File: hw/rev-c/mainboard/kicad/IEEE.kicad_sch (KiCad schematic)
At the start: 26 parts, among them J1 IEEE, J14 IEEE_HEADER, U14 SN74LS07, U15 SN74LS07, U16 SN74LS07, U17 74LS245, U18 74LS245

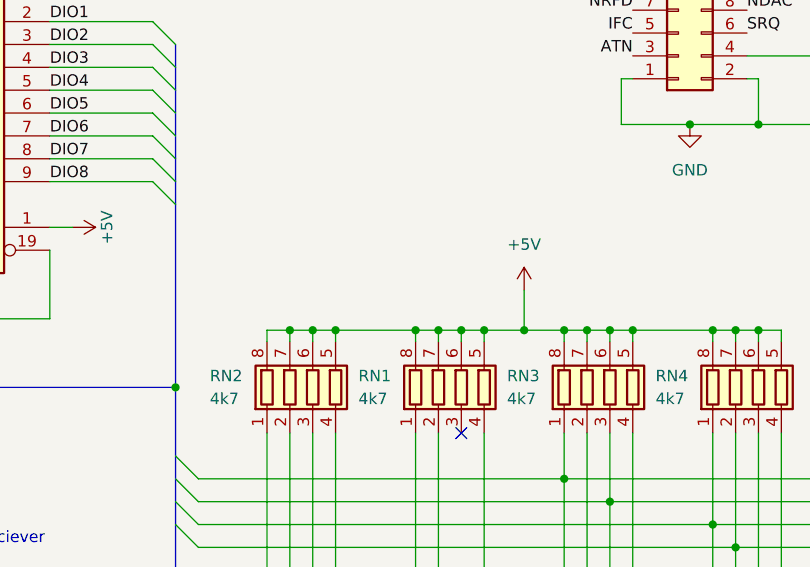
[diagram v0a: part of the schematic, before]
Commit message: hw: fix wire/grid violations in schematic
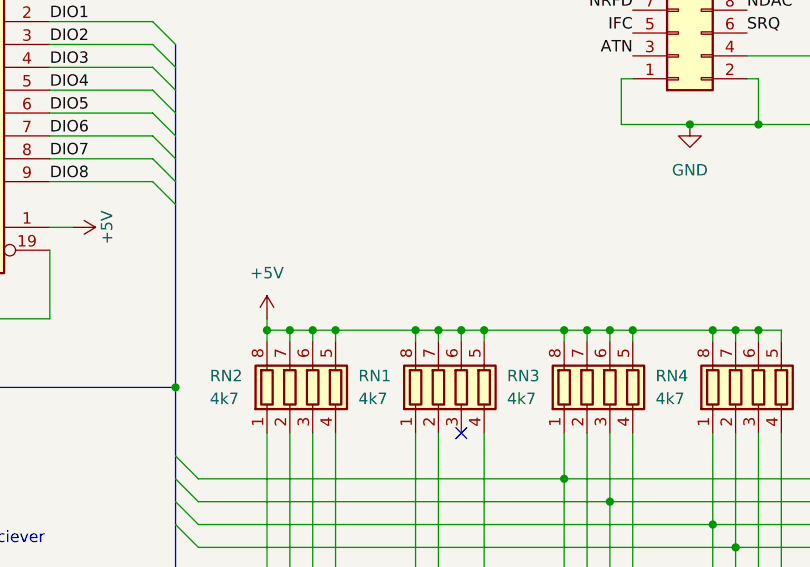
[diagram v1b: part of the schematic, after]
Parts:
- J1: symbol Retrocomputing:CBM_PET_IEEE_Conn_02x12_Card_Edge -> EconoPET:CBM_PET_IEEE_Conn_02x12_Card_Edge
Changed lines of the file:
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@@
 	)
 	(junction
-		(at 193.675 72.39)
-		(diameter 0)
-		(color 0 0 0 0)
-	)
-	(junction
 		(at 181.61 72.39)
 		(diameter 0)
@@
 	)
 	(junction
+		(at 165.1 72.39)
+		(diameter 0)
+		(color 0 0 0 0)
+	)
+	(junction
 		(at 198.12 88.9)
 		(diameter 0)
@@
 	(wire
 		(pts
+			(xy 165.1 72.39) (xy 167.64 72.39)
+		)
+		(stroke
+			(width 0)
+			(type default)
+		)
+	)
+	(wire
+		(pts
 			(xy 214.63 83.82) (xy 214.63 93.98)
 		)
@@
 		)
 	)
-	(wire
-		(pts
-			(xy 186.69 72.39) (xy 189.23 72.39)
-		)
-		(stroke
-			(width 0)
-			(type default)
-		)
-	)
 	(bus
 		(pts
@@
 	(wire
 		(pts
-			(xy 165.1 72.39) (xy 167.64 72.39)
-		)
-		(stroke
-			(width 0)
-			(type default)
-		)
-	)
-	(wire
-		(pts
 			(xy 140.97 172.72) (xy 143.51 172.72)
 		)
@@
 	(wire
 		(pts
-			(xy 189.23 72.39) (xy 193.675 72.39)
+			(xy 189.23 72.39) (xy 198.12 72.39)
 		)
 		(stroke
@@
 	(wire
 		(pts
-			(xy 193.675 67.945) (xy 193.675 72.39)
+			(xy 165.1 71.12) (xy 165.1 72.39)
 		)
 		(stroke
@@
 	(wire
 		(pts
-			(xy 181.61 72.39) (xy 184.15 72.39)
-		)
-		(stroke
-			(width 0)
-			(type default)
-		)
-	)
-	(wire
-		(pts
 			(xy 167.64 83.82) (xy 167.64 116.84)
 		)
@@
 		)
 	)
+	(wire
+		(pts
+			(xy 186.69 72.39) (xy 189.23 72.39)
+		)
+		(stroke
+			(width 0)
+			(type default)
+		)
+	)
 	(bus
 		(pts
@@
 	(wire
 		(pts
+			(xy 184.15 72.39) (xy 186.69 72.39)
+		)
+		(stroke
+			(width 0)
+			(type default)
+		)
+	)
+	(wire
+		(pts
 			(xy 140.97 40.64) (xy 152.4 40.64)
 		)
@@
 	(wire
 		(pts
-			(xy 172.72 72.39) (xy 172.72 73.66)
+			(xy 181.61 72.39) (xy 184.15 72.39)
 		)
 		(stroke
@@
 	(wire
 		(pts
-			(xy 259.08 91.44) (xy 203.2 91.44)
+			(xy 172.72 72.39) (xy 172.72 73.66)
 		)
 		(stroke
@@
 	(wire
 		(pts
-			(xy 193.675 72.39) (xy 198.12 72.39)
+			(xy 259.08 91.44) (xy 203.2 91.44)
 		)
 		(stroke
@@
 	(wire
 		(pts
-			(xy 184.15 72.39) (xy 186.69 72.39)
-		)
-		(stroke
-			(width 0)
-			(type default)
-		)
-	)
-	(wire
-		(pts
 			(xy 186.69 146.05) (xy 189.23 146.05)
 		)
@@
 	)
 	(symbol
-		(lib_id "Retrocomputing:CBM_PET_IEEE_Conn_02x12_Card_Edge")
+		(lib_id "EconoPET:CBM_PET_IEEE_Conn_02x12_Card_Edge")
 		(at 238.76 119.38 0)
 		(unit 1)
@@
 	(symbol
 		(lib_id "power:+5V")
-		(at 193.675 67.945 0)
+		(at 165.1 71.12 0)
 		(unit 1)
 		(exclude_from_sim no)
@@
 		(fields_autoplaced yes)
 		(property "Reference" "#PWR0111"
-			(at 193.675 71.755 0)
+			(at 165.1 74.93 0)
 			(effects
 				(font
@@
 		)
 		(property "Value" "+5V"
-			(at 193.675 62.865 0)
+			(at 165.1 66.04 0)
 			(effects
 				(font
@@
 		)
 		(property "Footprint" ""
-			(at 193.675 67.945 0)
+			(at 165.1 71.12 0)
 			(effects
 				(font
@@
 		)
 		(property "Datasheet" ""
-			(at 193.675 67.945 0)
+			(at 165.1 71.12 0)
 			(effects
 				(font
@@
 		)
 		(property "Description" "Power symbol creates a global label with name \"+5V\""
-			(at 193.675 67.945 0)
+			(at 165.1 71.12 0)
 			(effects
 				(font
@@
 	)
 	(symbol
-		(lib_id "PET:CHASSIS_GND")
+		(lib_id "EconoPET:CHASSIS_GND")
 		(at 232.41 135.89 0)
 		(unit 1)

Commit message: hw: more updates, move '07 to EconoPET
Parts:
- U14, U15, U16: symbol Mainboard-rescue:SN74LS07-PET -> EconoPET:SN74LS07
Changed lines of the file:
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@@
 	)
 	(symbol
-		(lib_id "Mainboard-rescue:SN74LS07-PET")
+		(lib_id "EconoPET:SN74LS07")
 		(at 69.85 182.88 0)
 		(unit 1)
@@
 	)
 	(symbol
-		(lib_id "Mainboard-rescue:SN74LS07-PET")
+		(lib_id "EconoPET:SN74LS07")
 		(at 69.85 101.6 0)
 		(unit 1)
@@
 	)
 	(symbol
-		(lib_id "Mainboard-rescue:SN74LS07-PET")
+		(lib_id "EconoPET:SN74LS07")
 		(at 69.85 55.88 0)
 		(unit 1)

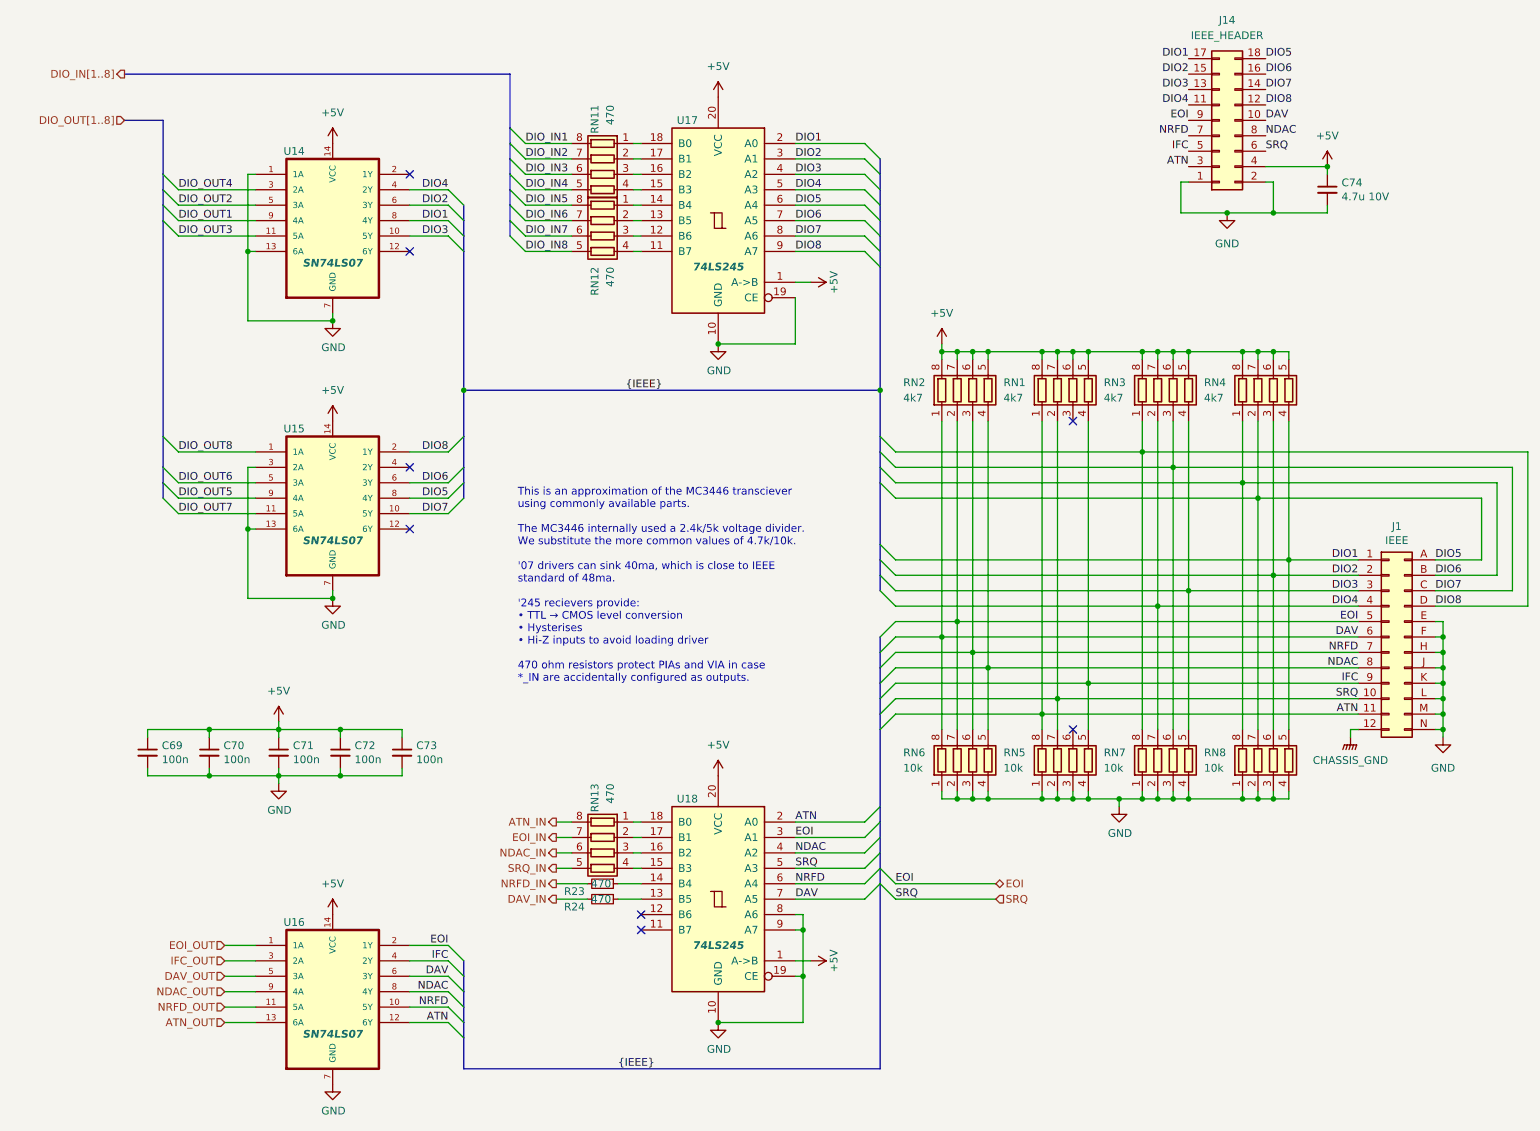
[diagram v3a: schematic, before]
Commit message: hw: renumber reference designators
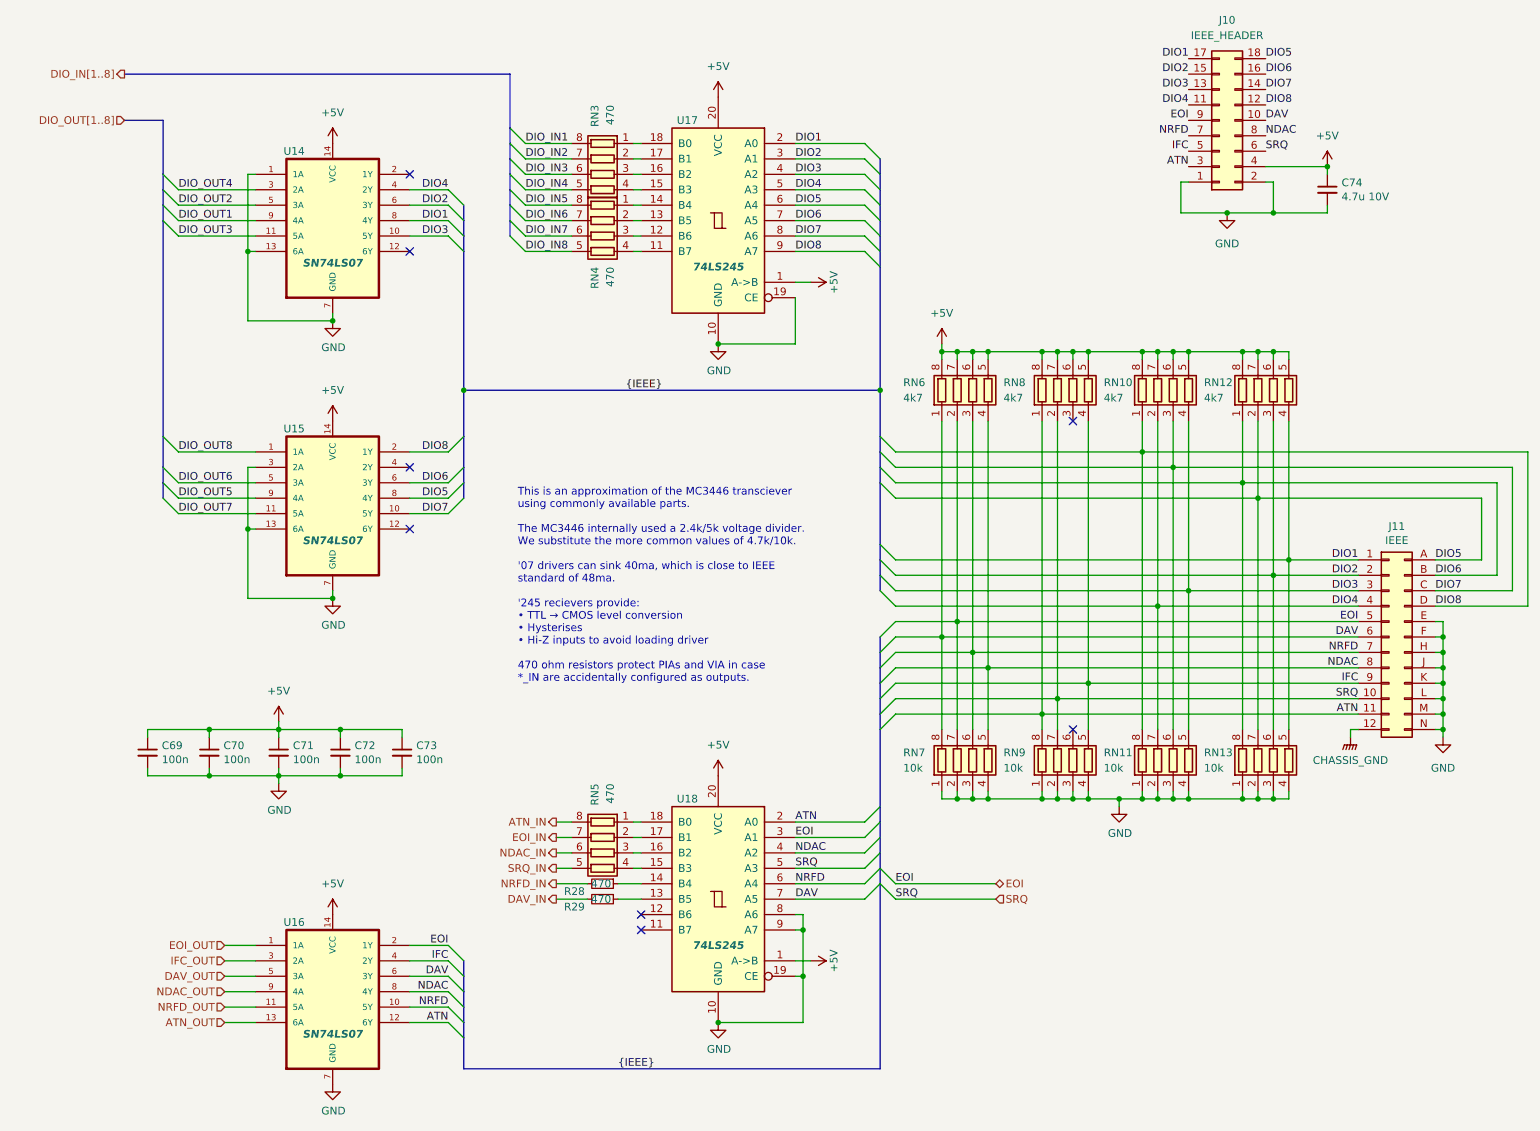
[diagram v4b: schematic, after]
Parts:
- renumbered J14 to J10, J1 to J11, R23 to R28, R24 to R29, RN3 to RN10, RN7 to RN11, RN4 to RN12, RN8 to RN13, RN11 to RN3, RN12 to RN4, RN13 to RN5, RN2 to RN6, RN6 to RN7, RN1 to RN8, RN5 to RN9
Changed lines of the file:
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@@
 		(on_board yes)
 		(dnp no)
-		(property "Reference" "J1"
+		(property "Reference" "J11"
 			(at 240.03 101.1682 0)
 			(effects
@@
 			(project ""
 				(path "/2eea20e6-112c-411a-b615-885ae773135a/00000000-0000-0000-0000-00006151ec26"
-					(reference "J1")
+					(reference "J11")
 					(unit 1)
 				)
@@
 		(on_board yes)
 		(dnp no)
-		(property "Reference" "R23"
+		(property "Reference" "R28"
 			(at 102.87 161.29 90)
 			(effects
@@
 			(project ""
 				(path "/2eea20e6-112c-411a-b615-885ae773135a/00000000-0000-0000-0000-00006151ec26"
-					(reference "R23")
+					(reference "R28")
 					(unit 1)
 				)
@@
 		(on_board yes)
 		(dnp no)
-		(property "Reference" "RN12"
+		(property "Reference" "RN4"
 			(at 107.95 58.42 0)
 			(effects
@@
 			(project ""
 				(path "/2eea20e6-112c-411a-b615-885ae773135a/00000000-0000-0000-0000-00006151ec26"
-					(reference "RN12")
+					(reference "RN4")
 					(unit 1)
 				)
@@
 		(on_board yes)
 		(dnp no)
-		(property "Reference" "RN6"
+		(property "Reference" "RN7"
 			(at 158.75 138.43 0)
 			(effects
@@
 			(project ""
 				(path "/2eea20e6-112c-411a-b615-885ae773135a/00000000-0000-0000-0000-00006151ec26"
-					(reference "RN6")
+					(reference "RN7")
 					(unit 1)
 				)
@@
 		(on_board yes)
 		(dnp no)
-		(property "Reference" "RN8"
+		(property "Reference" "RN13"
 			(at 208.28 138.43 0)
 			(effects
@@
 			(project ""
 				(path "/2eea20e6-112c-411a-b615-885ae773135a/00000000-0000-0000-0000-00006151ec26"
-					(reference "RN8")
+					(reference "RN13")
 					(unit 1)
 				)
@@
 		(dnp no)
 		(fields_autoplaced yes)
-		(property "Reference" "J14"
+		(property "Reference" "J10"
 			(at 212.09 17.78 0)
 			(effects
@@
 			(project ""
 				(path "/2eea20e6-112c-411a-b615-885ae773135a/00000000-0000-0000-0000-00006151ec26"
-					(reference "J14")
+					(reference "J10")
 					(unit 1)
 				)
@@
 		(on_board yes)
 		(dnp no)
-		(property "Reference" "RN4"
+		(property "Reference" "RN12"
 			(at 208.28 77.47 0)
 			(effects
@@
 			(project ""
 				(path "/2eea20e6-112c-411a-b615-885ae773135a/00000000-0000-0000-0000-00006151ec26"
-					(reference "RN4")
+					(reference "RN12")
 					(unit 1)
 				)
@@
 		(on_board yes)
 		(dnp no)
-		(property "Reference" "RN11"
+		(property "Reference" "RN3"
 			(at 107.95 31.75 0)
 			(effects
@@
 			(project ""
 				(path "/2eea20e6-112c-411a-b615-885ae773135a/00000000-0000-0000-0000-00006151ec26"
-					(reference "RN11")
+					(reference "RN3")
 					(unit 1)
 				)
@@
 		(on_board yes)
 		(dnp no)
-		(property "Reference" "RN5"
+		(property "Reference" "RN9"
 			(at 175.26 138.43 0)
 			(effects
@@
 			(project ""
 				(path "/2eea20e6-112c-411a-b615-885ae773135a/00000000-0000-0000-0000-00006151ec26"
-					(reference "RN5")
+					(reference "RN9")
 					(unit 1)
 				)
@@
 		(on_board yes)
 		(dnp no)
-		(property "Reference" "RN13"
+		(property "Reference" "RN5"
 			(at 107.95 143.51 0)
 			(effects
@@
 			(project ""
 				(path "/2eea20e6-112c-411a-b615-885ae773135a/00000000-0000-0000-0000-00006151ec26"
-					(reference "RN13")
+					(reference "RN5")
 					(unit 1)
 				)
@@
 		(on_board yes)
 		(dnp no)
-		(property "Reference" "RN1"
+		(property "Reference" "RN8"
 			(at 175.26 77.47 0)
 			(effects
@@
 			(project ""
 				(path "/2eea20e6-112c-411a-b615-885ae773135a/00000000-0000-0000-0000-00006151ec26"
-					(reference "RN1")
+					(reference "RN8")
 					(unit 1)
 				)
@@
 		(on_board yes)
 		(dnp no)
-		(property "Reference" "RN2"
+		(property "Reference" "RN6"
 			(at 158.75 77.47 0)
 			(effects
@@
 			(project ""
 				(path "/2eea20e6-112c-411a-b615-885ae773135a/00000000-0000-0000-0000-00006151ec26"
-					(reference "RN2")
+					(reference "RN6")
 					(unit 1)
 				)
@@
 		(on_board yes)
 		(dnp no)
-		(property "Reference" "R24"
+		(property "Reference" "R29"
 			(at 102.87 163.83 90)
 			(effects
@@
 			(project ""
 				(path "/2eea20e6-112c-411a-b615-885ae773135a/00000000-0000-0000-0000-00006151ec26"
-					(reference "R24")
+					(reference "R29")
 					(unit 1)
 				)
@@
 		(on_board yes)
 		(dnp no)
-		(property "Reference" "RN7"
+		(property "Reference" "RN11"
 			(at 191.77 138.43 0)
 			(effects
@@
 			(project ""
 				(path "/2eea20e6-112c-411a-b615-885ae773135a/00000000-0000-0000-0000-00006151ec26"
-					(reference "RN7")
+					(reference "RN11")
 					(unit 1)
 				)
@@
 		(on_board yes)
 		(dnp no)
-		(property "Reference" "RN3"
+		(property "Reference" "RN10"
 			(at 191.77 77.47 0)
 			(effects
@@
 			(project ""
 				(path "/2eea20e6-112c-411a-b615-885ae773135a/00000000-0000-0000-0000-00006151ec26"
-					(reference "RN3")
-					(unit 1)
-				)
+					(reference "RN10")
+					(unit 1)
+				)
